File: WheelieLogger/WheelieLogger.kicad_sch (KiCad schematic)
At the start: 33 parts, among them J1 USB_C_Plug_USB2.0, J2 Conn_Power, J3 Conn_GPIO, SW1 SW_RESET, U1 GD25Q32CNIGR, U2 MCP1700-3302E_SOT23, U3 ATSAMD21E18A, U4 MPU-6050

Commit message: Draft of SerpenteR2 board instructions
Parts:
- removed J2: Conn_Power, Connector_PinHeader_2.54mm_Extra:PinHeader_1x04_P2.54mm_Vertical_Castellated, symbol Connector_Generic:Conn_01x04
- removed J3: Conn_GPIO, Connector_PinHeader_2.54mm_Extra:PinHeader_1x06_P2.54mm_Vertical_Castellated, symbol Connector_Generic:Conn_01x06
- added J2: Conn_Power, Connector_JST:JST_PH_B2B-PH-SM4-TB_1x02-1MP_P2.00mm_Vertical, symbol Connector_Generic:Conn_01x02
- added SW2: SW_DIP_x02, Package_DIP:SMDIP-4_W7.62mm, symbol Switch:SW_DIP_x02
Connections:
- net GND: now also J2.2 (Pin_2), SW2.1
- net GPIO3: now also SW2.4
- net VIN: now also SW2.3
- net GPIO0: no longer names the net of U3.5 (PA04)
- net GPIO1: no longer names the net of U3.6 (PA05)
- net GPIO2: no longer names the net of U3.7 (PA06)
- new net PWR_SW: J2.1 (Pin_1), SW2.2
- no-connect marks 16 -> 19
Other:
- moved on the sheet: C2, C3, C4, C5, C6, C7, C8, R6, SW1, TP1, TP2, TP5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

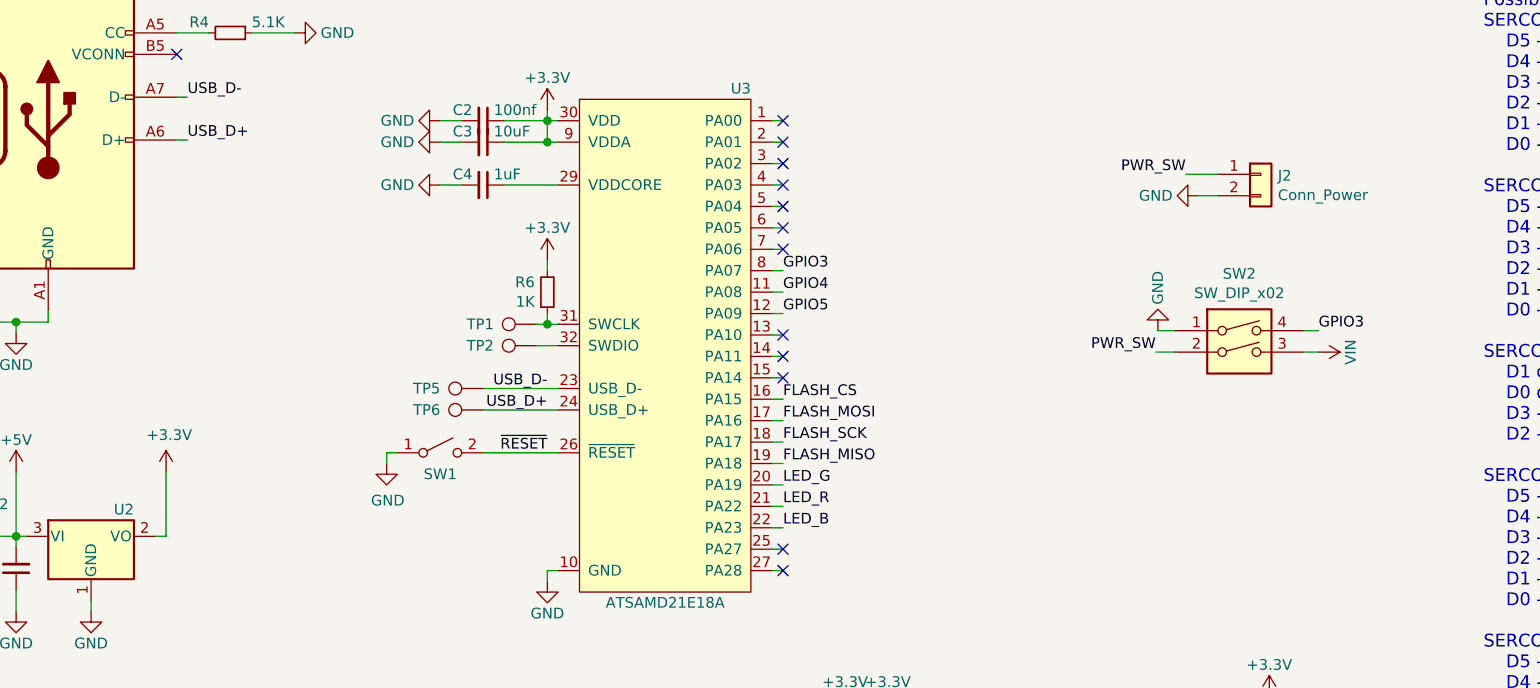
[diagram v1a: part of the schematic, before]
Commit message: 1.Added 1uF cap to pin2 of the MCP1700 (U2) 2.Removed dip switches, replaced with DPDT slide switch as they should always operate together 3.Updated the JST-PH connector from an SMD to a through-hole unit 4.Updated the footprint of the USB-C connector
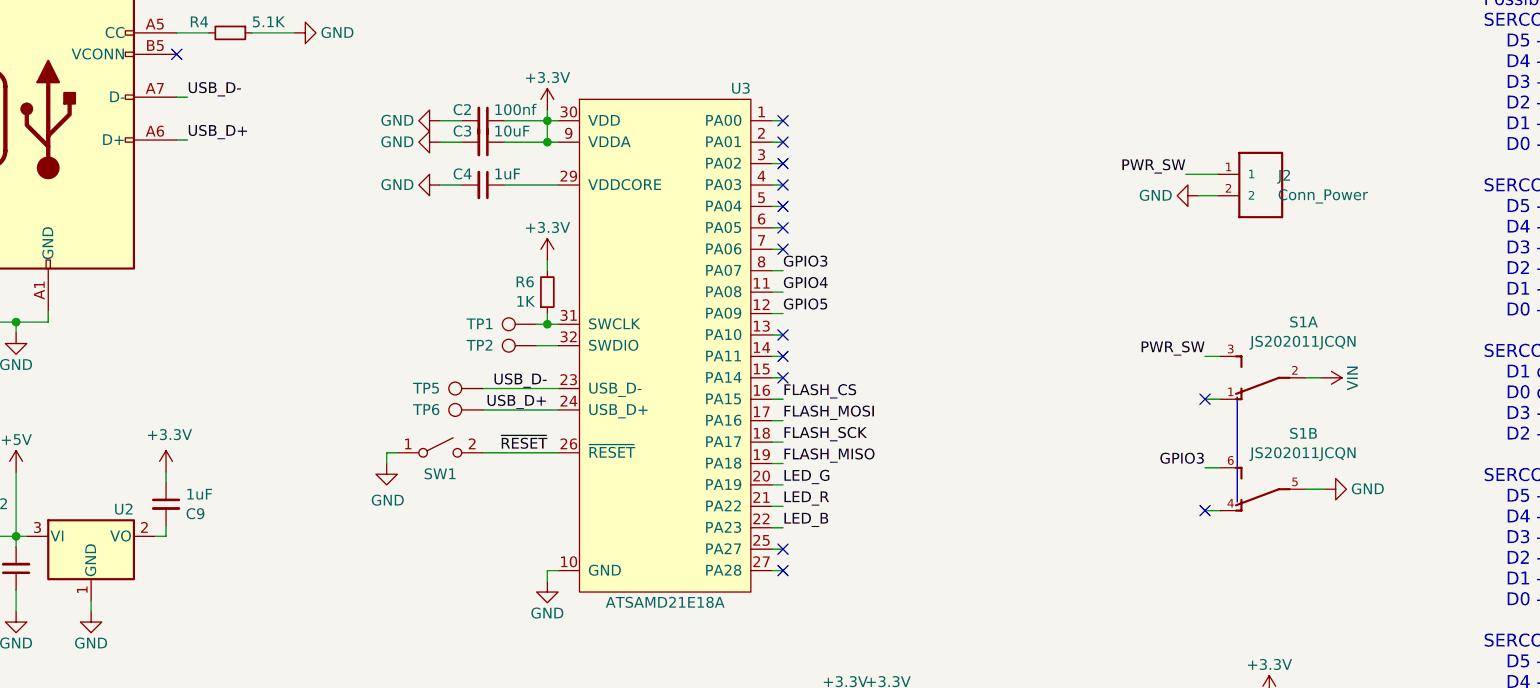
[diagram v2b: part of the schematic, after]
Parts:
- removed SW2: SW_DIP_x02, Package_DIP:SMDIP-4_W7.62mm, symbol Switch:SW_DIP_x02
- added C9: 1uF, Capacitor_SMD:C_0402_1005Metric, symbol Device:C_Small
- added S1: JS202011JCQN, Button_Switch_THT:SW_CuK_JS202011CQN_DPDT_Straight, symbol JS202011JCQN:JS202011JCQN
- C1, C4: Est Unit Cost 0.57 -> (none); price (none) -> 0.57
- C2, C7: Est Unit Cost 0.12 -> (none); price (none) -> 0.12
- C3: Est Unit Cost 0.59 -> (none); price (none) -> 0.59
- C5, C6: Est Unit Price 0.12 -> (none); price (none) -> 0.12
- C8: Est Unit Price 0.19 -> (none); price (none) -> 0.19
- D3, SW1: Est Unit Cost 0.41 -> (none); price (none) -> 0.41
- J1: footprint Connector_USB_Extra:USB_C_Plug_UTC009-C12 -> Connector_USB:USB_C_Receptacle_XKB_U262-16XN-4BVC11; Est Unit Cost 0.34 -> (none); price (none) -> 0.34
- J2: footprint Connector_JST:JST_PH_B2B-PH-SM4-TB_1x02-1MP_P2.00mm_Vertical -> Connector_JST:JST_PH_B2B-PH-K_1x02_P2.00mm_Vertical; symbol Connector_Generic:Conn_01x02 -> B2B-PH-SM4-TB_LF__SN_:B2B-PH-SM4-TB(LF)(SN); Est Unit Cost 0.15 -> (none); LCSC Part # C160352 -> C131337; Manufacturer Part # B2B-PH-SM4-TB(LF)(SN) -> B2B-PH-K-S(LF)(SN); Package SMD,P=2mm -> Through Hole; price (none) -> 0.54
- U1: Est Unit Price 1.3 -> (none); price (none) -> 1.3
- U2: Est Unit Cost 0.31 -> (none); price (none) -> 0.31
- U3: Est Unit Cost 4.1 -> (none); price (none) -> 4.1
- U4: Est Unit Price 2.57 -> (none); price (none) -> 2.57
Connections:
- net +3V3: now also C9.1; no longer U2.2 (VO)
- net GND: now also S1.5
- net GPIO3: now also S1.6
- net PWR_SW: now also S1.3
- net VIN: now also S1.2
- new net: C9.2, U2.2 (VO)
- no-connect marks 19 -> 21

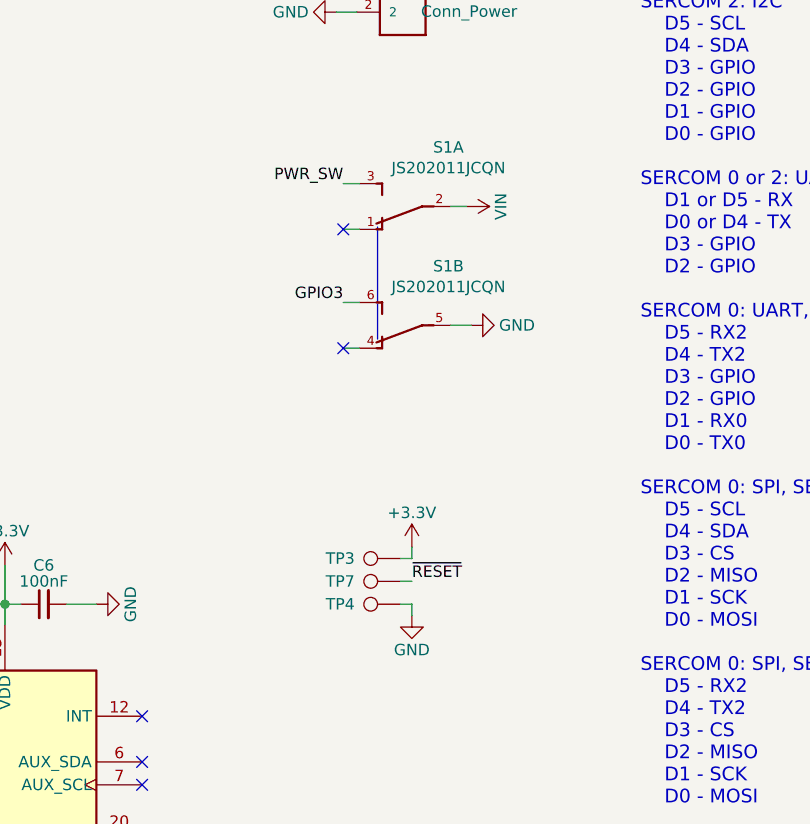
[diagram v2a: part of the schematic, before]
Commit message: Rebuilt the tracks in the PCB Removed some test points
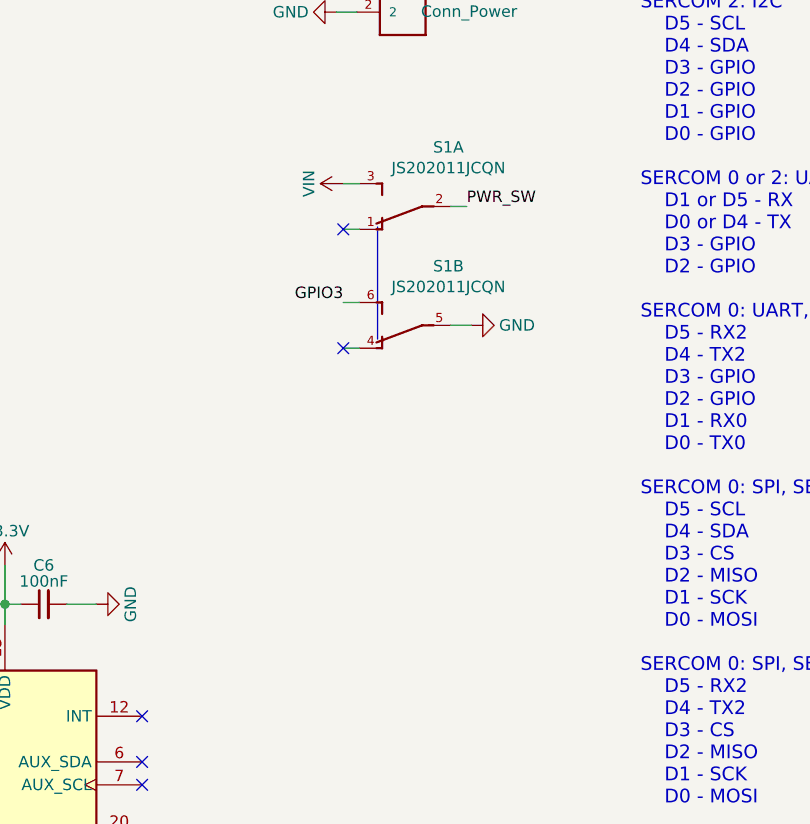
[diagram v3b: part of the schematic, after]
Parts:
- removed TP3: TP_VDD, TestPoint:TestPoint_Pad_D1.0mm, symbol Connector:TestPoint
- removed TP4: TP_GND, TestPoint:TestPoint_Pad_D1.0mm, symbol Connector:TestPoint
- removed TP7: TP_RESET, TestPoint:TestPoint_Pad_D1.0mm, symbol Connector:TestPoint
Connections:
- net PWR_SW: now also S1.2; no longer S1.3
- net VIN: now also S1.3; no longer S1.2
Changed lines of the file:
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@@
   (junction (at 149.098 111.76) (diameter 1.016) (color 0 0 0 0))
   (junction (at 154.178 111.76) (diameter 1.016) (color 0 0 0 0))
-  (no_connect (at 169.418 124.206))
+  (no_connect (at 141.732 67.564))
+  (no_connect (at 141.732 87.884))
+  (no_connect (at 141.732 90.424))
+  (no_connect (at 191.77 70.104))
+  (no_connect (at 69.85 29.21))
+  (no_connect (at 141.732 44.704))
+  (no_connect (at 141.732 39.624))
+  (no_connect (at 141.732 42.164))
+  (no_connect (at 169.418 131.826))
+  (no_connect (at 191.77 83.312))
   (no_connect (at 133.858 139.446))
-  (no_connect (at 141.732 47.244))
-  (no_connect (at 191.77 70.104))
-  (no_connect (at 191.77 83.312))
-  (no_connect (at 169.418 131.826))
-  (no_connect (at 141.732 90.424))
-  (no_connect (at 141.732 52.324))
-  (no_connect (at 141.732 37.084))
-  (no_connect (at 141.732 44.704))
-  (no_connect (at 133.858 136.906))
-  (no_connect (at 141.732 39.624))
   (no_connect (at 141.732 62.484))
   (no_connect (at 169.418 129.286))
+  (no_connect (at 141.732 49.784))
+  (no_connect (at 141.732 65.024))
+  (no_connect (at 141.732 47.244))
+  (no_connect (at 133.858 136.906))
+  (no_connect (at 141.732 52.324))
+  (no_connect (at 169.418 124.206))
+  (no_connect (at 141.732 37.084))
   (no_connect (at 133.858 129.286))
-  (no_connect (at 141.732 87.884))
-  (no_connect (at 141.732 65.024))
-  (no_connect (at 141.732 49.784))
-  (no_connect (at 141.732 67.564))
-  (no_connect (at 141.732 42.164))
-  (no_connect (at 69.85 29.21))
   (wire (pts (xy 40.64 80.01) (xy 40.64 78.74))
     (stroke (width 0) (type solid) (color 0 0 0 0))
@@
   )
   (wire (pts (xy 191.77 83.312) (xy 193.548 83.312))
-    (stroke (width 0) (type solid) (color 0 0 0 0))
-  )
-  (wire (pts (xy 198.12 106.68) (xy 199.39 106.68))
-    (stroke (width 0) (type solid) (color 0 0 0 0))
-  )
-  (wire (pts (xy 198.12 109.22) (xy 199.39 109.22))
-    (stroke (width 0) (type solid) (color 0 0 0 0))
-  )
-  (wire (pts (xy 198.12 111.76) (xy 199.39 111.76))
-    (stroke (width 0) (type solid) (color 0 0 0 0))
-  )
-  (wire (pts (xy 199.39 106.68) (xy 199.39 105.41))
-    (stroke (width 0) (type solid) (color 0 0 0 0))
-  )
-  (wire (pts (xy 199.39 111.76) (xy 199.39 113.03))
     (stroke (width 0) (type solid) (color 0 0 0 0))
   )
@@
     (effects (font (size 1.27 1.27)) (justify right bottom))
   )
-  (label "PWR_SW" (at 191.77 65.024 180)
-    (effects (font (size 1.27 1.27)) (justify right bottom))
-  )
   (label "GPIO3" (at 191.77 78.232 180)
     (effects (font (size 1.27 1.27)) (justify right bottom))
   )
-  (label "~RESET~" (at 199.39 109.22 0)
+  (label "PWR_SW" (at 205.486 67.564 0)
     (effects (font (size 1.27 1.27)) (justify left bottom))
   )
@@
     )
   )
-  (symbol (lib_id "Connector:TestPoint") (at 198.12 106.68 90) (unit 1)
-    (in_bom yes) (on_board yes)
-    (property "Reference" "TP3" (id 0) (at 193.04 106.68 90)
-      (effects (font (size 1.27 1.27)) (justify left))
-    )
-    (property "Value" "TP_VDD" (id 1) (at 196.2912 104.0384 90)
-      (effects (font (size 1.27 1.27)) hide)
-    )
-    (property "Footprint" "TestPoint:TestPoint_Pad_D1.0mm" (id 2) (at 198.12 101.6 0)
-      (effects (font (size 1.27 1.27)) hide)
-    )
-    (property "Datasheet" "~" (id 3) (at 198.12 101.6 0)
-      (effects (font (size 1.27 1.27)) hide)
-    )
-  )
-  (symbol (lib_id "Connector:TestPoint") (at 198.12 109.22 90) (unit 1)
-    (in_bom yes) (on_board yes)
-    (property "Reference" "TP7" (id 0) (at 193.04 109.22 90)
-      (effects (font (size 1.27 1.27)) (justify left))
-    )
-    (property "Value" "TP_RESET" (id 1) (at 196.2912 106.5784 90)
-      (effects (font (size 1.27 1.27)) hide)
-    )
-    (property "Footprint" "TestPoint:TestPoint_Pad_D1.0mm" (id 2) (at 198.12 104.14 0)
-      (effects (font (size 1.27 1.27)) hide)
-    )
-    (property "Datasheet" "~" (id 3) (at 198.12 104.14 0)
-      (effects (font (size 1.27 1.27)) hide)
-    )
-  )
-  (symbol (lib_id "Connector:TestPoint") (at 198.12 111.76 90) (unit 1)
-    (in_bom yes) (on_board yes)
-    (property "Reference" "TP4" (id 0) (at 193.04 111.76 90)
-      (effects (font (size 1.27 1.27)) (justify left))
-    )
-    (property "Value" "TP_GND" (id 1) (at 196.2912 109.1184 90)
-      (effects (font (size 1.27 1.27)) hide)
-    )
-    (property "Footprint" "TestPoint:TestPoint_Pad_D1.0mm" (id 2) (at 198.12 106.68 0)
-      (effects (font (size 1.27 1.27)) hide)
-    )
-    (property "Datasheet" "~" (id 3) (at 198.12 106.68 0)
-      (effects (font (size 1.27 1.27)) hide)
-    )
-  )
   (symbol (lib_id "power:VBUS") (at 40.64 78.74 0) (unit 1)
     (in_bom yes) (on_board yes)
@@
     )
   )
-  (symbol (lib_id "power:+3.3V") (at 199.39 105.41 0) (unit 1)
-    (in_bom yes) (on_board yes)
-    (property "Reference" "#PWR022" (id 0) (at 199.39 109.22 0)
-      (effects (font (size 1.27 1.27)) hide)
-    )
-    (property "Value" "+3.3V" (id 1) (at 199.39 101.6 0))
-    (property "Footprint" "" (id 2) (at 199.39 105.41 0)
-      (effects (font (size 1.27 1.27)) hide)
-    )
-    (property "Datasheet" "" (id 3) (at 199.39 105.41 0)
-      (effects (font (size 1.27 1.27)) hide)
-    )
-  )
-  (symbol (lib_id "WheelieLogger-rescue:VIN-power_extra-serpente_plug_c-rescue") (at 205.486 67.564 270) (unit 1)
-    (in_bom yes) (on_board yes)
-    (property "Reference" "#PWR014" (id 0) (at 201.676 67.564 0)
-      (effects (font (size 1.27 1.27)) hide)
-    )
-    (property "Value" "VIN" (id 1) (at 209.296 67.564 0))
-    (property "Footprint" "" (id 2) (at 205.486 67.564 0)
-      (effects (font (size 1.27 1.27)) hide)
-    )
-    (property "Datasheet" "" (id 3) (at 205.486 67.564 0)
+  (symbol (lib_id "WheelieLogger-rescue:VIN-power_extra-serpente_plug_c-rescue") (at 191.77 65.024 90) (unit 1)
+    (in_bom yes) (on_board yes)
+    (property "Reference" "#PWR014" (id 0) (at 195.58 65.024 0)
+      (effects (font (size 1.27 1.27)) hide)
+    )
+    (property "Value" "VIN" (id 1) (at 187.96 65.024 0))
+    (property "Footprint" "" (id 2) (at 191.77 65.024 0)
+      (effects (font (size 1.27 1.27)) hide)
+    )
+    (property "Datasheet" "" (id 3) (at 191.77 65.024 0)
       (effects (font (size 1.27 1.27)) hide)
     )
@@
     )
     (property "Datasheet" "" (id 3) (at 191.008 45.974 0)
-      (effects (font (size 1.27 1.27)) hide)
-    )
-  )
-  (symbol (lib_id "power:GND") (at 199.39 113.03 0) (unit 1)
-    (in_bom yes) (on_board yes)
-    (property "Reference" "#PWR023" (id 0) (at 199.39 119.38 0)
-      (effects (font (size 1.27 1.27)) hide)
-    )
-    (property "Value" "GND" (id 1) (at 199.39 116.84 0))
-    (property "Footprint" "" (id 2) (at 199.39 113.03 0)
-      (effects (font (size 1.27 1.27)) hide)
-    )
-    (property "Datasheet" "" (id 3) (at 199.39 113.03 0)
       (effects (font (size 1.27 1.27)) hide)
     )
@@
       (reference "#PWR021") (unit 1)
     )
-    (path "/00000000-0000-0000-0000-00005d613a09"
-      (reference "#PWR022") (unit 1)
-    )
-    (path "/00000000-0000-0000-0000-00005d6136b1"
-      (reference "#PWR023") (unit 1)
-    )
     (path "/00000000-0000-0000-0000-00005d7c7be6"
       (reference "#PWR0101") (unit 1)
@@
       (reference "TP2") (unit 1)
     )
-    (path "/00000000-0000-0000-0000-00005d60d63c"
-      (reference "TP3") (unit 1)
-    )
-    (path "/00000000-0000-0000-0000-00005d60e018"
-      (reference "TP4") (unit 1)
-    )
     (path "/00000000-0000-0000-0000-00005d6c95ec"
       (reference "TP5") (unit 1)
@@
       (reference "TP6") (unit 1)
     )
-    (path "/00000000-0000-0000-0000-00005d8ed0c1"
-      (reference "TP7") (unit 1)
-    )
     (path "/00000000-0000-0000-0000-00005d58bc09"

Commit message: Improved bottom layer GND mask Added part numbers for D1 and D2 Tidy up top and bottom silk screen layers
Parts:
- C1, C4, C9: LCSC (none) -> C115046; LCSC Part # C115046 -> (none); Manufacturer YAGEO -> (none); Manufacturer Part # CC0402KRX7R5BB105 -> (none); vendor (none) -> YAGEO; vendor part # (none) -> CC0402KRX7R5BB105
- C2, C6: LCSC (none) -> C541406; LCSC Part # C541406 -> (none); Manufacturer YAGEO -> (none); Manufacturer Part # CC0402KRX7R5BB104 -> (none); vendor (none) -> YAGEO; vendor part # (none) -> CC0402KRX7R5BB104
- C3: LCSC (none) -> C105884; LCSC Part # C105884 -> (none); Manufacturer YAGEO -> (none); Manufacturer Part # CC0402MRX5R5BB106 -> (none); vendor (none) -> YAGEO; vendor part # (none) -> CC0402MRX5R5BB106
- C5: LCSC (none) -> C541370; LCSC Part # C541370 -> (none); Manufacturer YAGEO -> (none); Manufacturer Part # CC0402KRX7R5BB103 -> (none); vendor (none) -> YAGEO; vendor part # (none) -> CC0402KRX7R5BB103
- C7: LCSC (none) -> C541406; LCSC Part# C541406 -> (none); Manufacturer YAGEO -> (none); Manufacturer Part # CC0402KRX7R5BB104 -> (none); vendor (none) -> YAGEO; vendor part # (none) -> CC0402KRX7R5BB104
- C8: LCSC (none) -> C106861; LCSC Part # C106861 -> (none); Manufacturer YAGEO -> (none); Manufacturer Part # CC0402KRX7R9BB222 -> (none); vendor (none) -> YAGEO; vendor part # (none) -> CC0402KRX7R9BB222
- D1, D2: LCSC (none) -> C114023; Package (none) -> SOD-323; price (none) -> 0.39; vendor (none) -> MDD(Microdiode Electronics); vendor part # (none) -> B5817WS-SJ
- D3: LCSC (none) -> C727904; LCSC Part # C727904 -> (none); Manufacturer Foshan NationStar Optoelectronics -> (none); Manufacturer Part # FM-B1921RGBA-SH -> (none); vendor (none) -> Foshan NationStar Optoelectronics; vendor part # (none) -> FM-B1921RGBA-SH
- J1: LCSC (none) -> C319148; LCSC Part # C319148 -> (none); Manufacturer XKB Connectivity -> (none); Manufacturer Part # U262-161N-4BVC11 -> (none); vendor (none) -> XKB Connectivity; vendor part # (none) -> U262-161N-4BVC11
- J2: LCSC (none) -> C131337; LCSC Part # C131337 -> (none); Manufacturer JST Sales America -> (none); Manufacturer Part # B2B-PH-K-S(LF)(SN) -> (none); vendor (none) -> JST Sales America; vendor part # (none) -> B2B-PH-K-S(LF)(SN)
- S1: LCSC (none) -> C221665; Package (none) -> SMD; price (none) -> 0.56; vendor (none) -> C&K; vendor part # (none) -> JS202011JCQN
- SW1: LCSC (none) -> C231330; LCSC Part # C231330 -> (none); Manufacturer Omron Electronics -> (none); Manufacturer Part # B3U-1000P-B -> (none); vendor (none) -> Omron Electronics; vendor part # (none) -> B3U-1000P-B
- U1: LCSC (none) -> C395491; LCSC Part # C395491 -> (none); Manufacturer GigaDevice Semicon Beijing -> (none); Manufacturer Part # GD25Q32CNIGR -> (none); vendor (none) -> GigaDevice Semicon Beijing; vendor part # (none) -> GD25Q32CNIGR
- U2: LCSC (none) -> C39051; LCSC Part # C39051 -> (none); Manufacturer Microchip Tech -> (none); Manufacturer Part # MCP1700T-3302E/TT -> (none); vendor (none) -> Microchip Tech; vendor part # (none) -> MCP1700T-3302E/TT
- U3: LCSC (none) -> C220692; LCSC Part # C220692 -> (none); Manufacturer Microchip Tech -> (none); Manufacturer Part # ATSAMD21E18A-MU -> (none); vendor (none) -> Microchip Tech; vendor part # (none) -> ATSAMD21E18A-MU
- U4: LCSC (none) -> C24112; LCSC Datasheet https://datasheet.lcsc.com/szlcsc/1811071024_TDK-InvenSense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 -> (none); LCSC Part # C24112 -> (none); Manufacturer Part # MPU-6050 -> (none); vendor (none) -> tdk; vendor part # (none) -> MPU-6050
